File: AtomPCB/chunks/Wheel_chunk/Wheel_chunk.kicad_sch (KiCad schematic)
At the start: 31 parts, among them J1 DF40HC_4.0_-40DS-0.4V_70_, J2 Conn_01x04_Pin, J3 Conn_01x04_Pin, J4 Conn_01x04_Pin, J5 Conn_01x04_Pin, U1 ATtiny416-M, U3 DRV8834RGER, U4 DRV8834RGER, U6 MPM3610AGQV-P

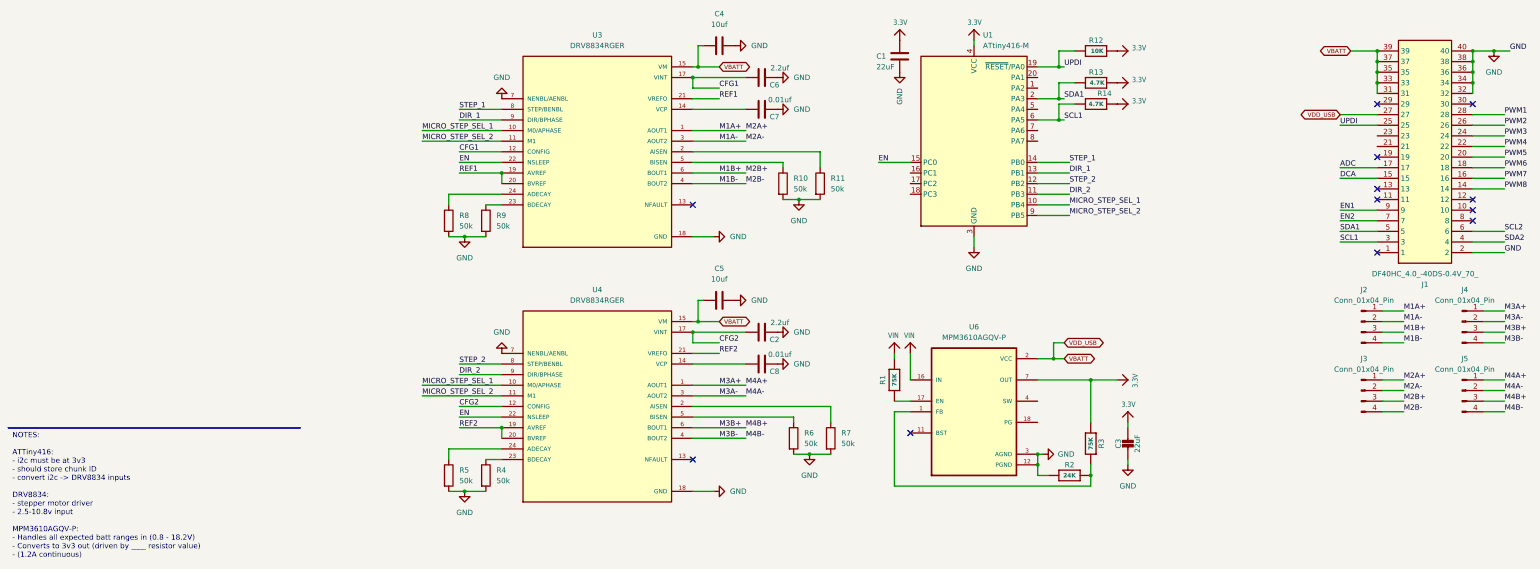
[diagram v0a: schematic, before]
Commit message: adding wheel chunk updates, fixing buck wiring issues
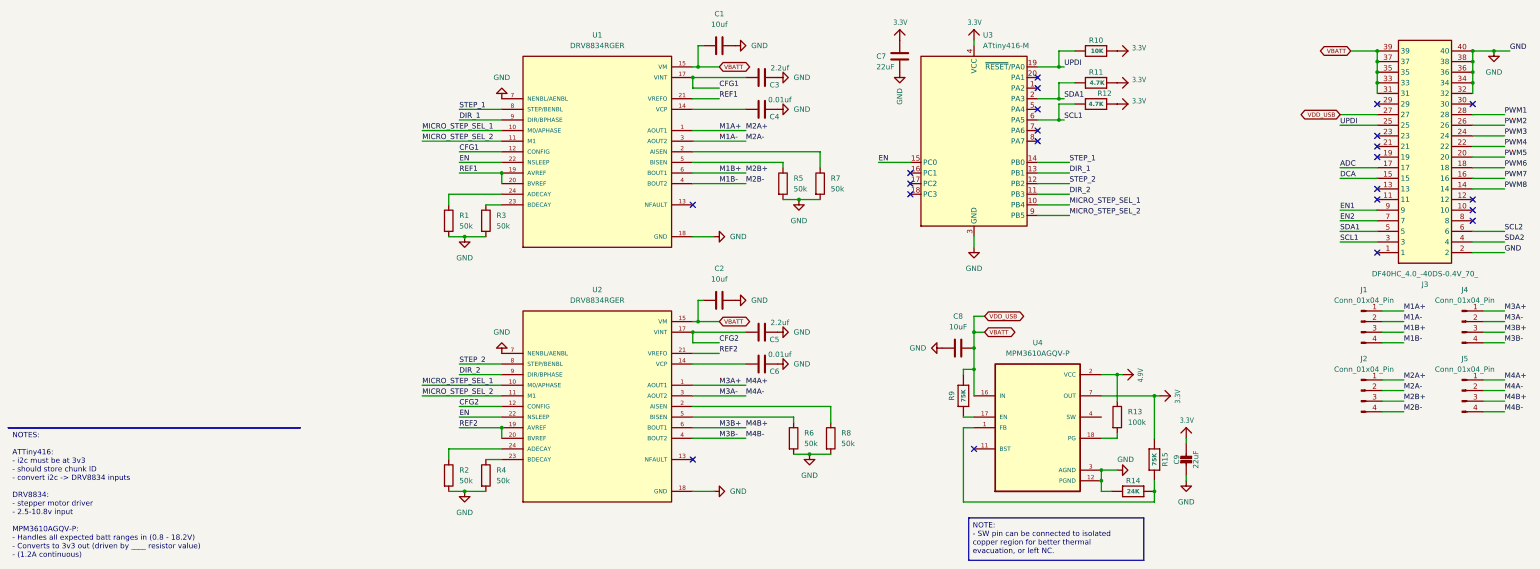
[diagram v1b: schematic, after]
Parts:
- removed C3: 22uF, Capacitor_SMD:C_0805_2012Metric, symbol Wheel_chunk-eagle-import:CAP_CERAMIC0805-NOOUTLINE
- removed R1, R3: 75K, Resistor_SMD:R_0805_2012Metric, symbol Wheel_chunk-eagle-import:RESISTOR_0603_NOOUT
- removed R2: 24K, Resistor_SMD:R_0805_2012Metric, symbol Wheel_chunk-eagle-import:RESISTOR_0603_NOOUT
- removed U6: MPM3610AGQV-P, MPM3610AGQV-P:CONV_MPM3620AGQV-P, symbol MPM3610AGQV-P:MPM3610AGQV-P
- added C8: 10uF, Capacitor_SMD:C_0805_2012Metric, symbol Device:C
- added C9: 22uF, Capacitor_SMD:C_0805_2012Metric, symbol Wheel_chunk-eagle-import:CAP_CERAMIC0805-NOOUTLINE
- added R13: 100k, Resistor_SMD:R_0805_2012Metric, symbol Device:R
- added R14: 24K, Resistor_SMD:R_0805_2012Metric, symbol Wheel_chunk-eagle-import:RESISTOR_0603_NOOUT
- added R15, R9: 75K, Resistor_SMD:R_0805_2012Metric, symbol Wheel_chunk-eagle-import:RESISTOR_0603_NOOUT
- added U4: MPM3610AGQV-P, MPM3610AGQV-P:CONV_MPM3620AGQV-P, symbol MPM3610AGQV-P:MPM3610AGQV-P
- renumbered C4 to C1, C5 to C2, C6 to C3, C7 to C4, C2 to C5, C8 to C6, C1 to C7, J2 to J1, J3 to J2, J1 to J3, R8 to R1, R12 to R10, R13 to R11, R14 to R12, R5 to R2, R9 to R3, R10 to R5, R11 to R7, R7 to R8, U3 to U1, U4 to U2, U1 to U3
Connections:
- net 3.3V: now also C9.1, R15.1, U4.20 (OUT), U4.7 (OUT), U4.8 (OUT), U4.9 (OUT)
- net GND: now also C8.1, C9.2, R14.1, U4.12 (PGND), U4.13 (PGND), U4.14 (PGND), U4.3 (AGND)
- net VM: now also C8.2, R9.1, U4.16 (IN)
- new net: R14.2, R15.2, U4.1 (FB)
- new net: R9.2, U4.17 (EN)
- new net: R13.2, U4.18 (PG)
- new net: U4.19 (SW), U4.4 (SW), U4.5 (SW), U4.6 (SW)
- new net 4.9V: R13.1, U4.2 (VCC)
- no-connect marks 12 -> 22
